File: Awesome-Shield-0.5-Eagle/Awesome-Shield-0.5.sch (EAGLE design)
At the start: 24 parts, among them J1 ARDUINO_R3_SHIELDUNO_R3_SHIEL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, SW1 SPST_TACT-EVQQ2

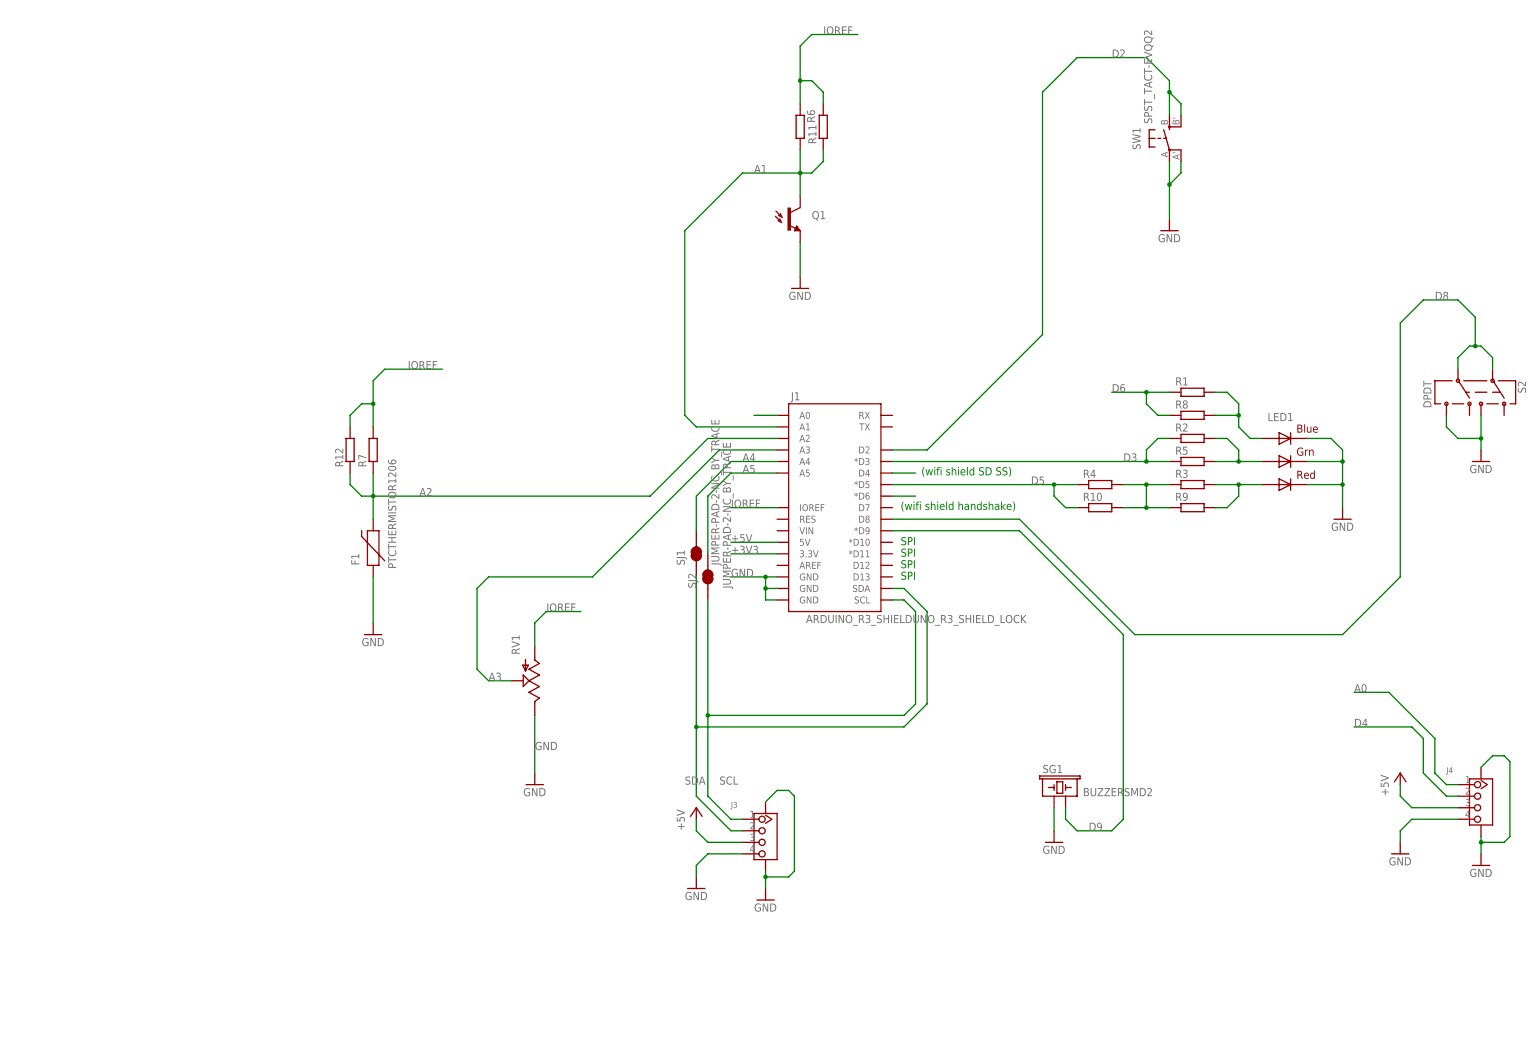
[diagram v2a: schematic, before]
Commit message: switched locking headers board for normal headers board
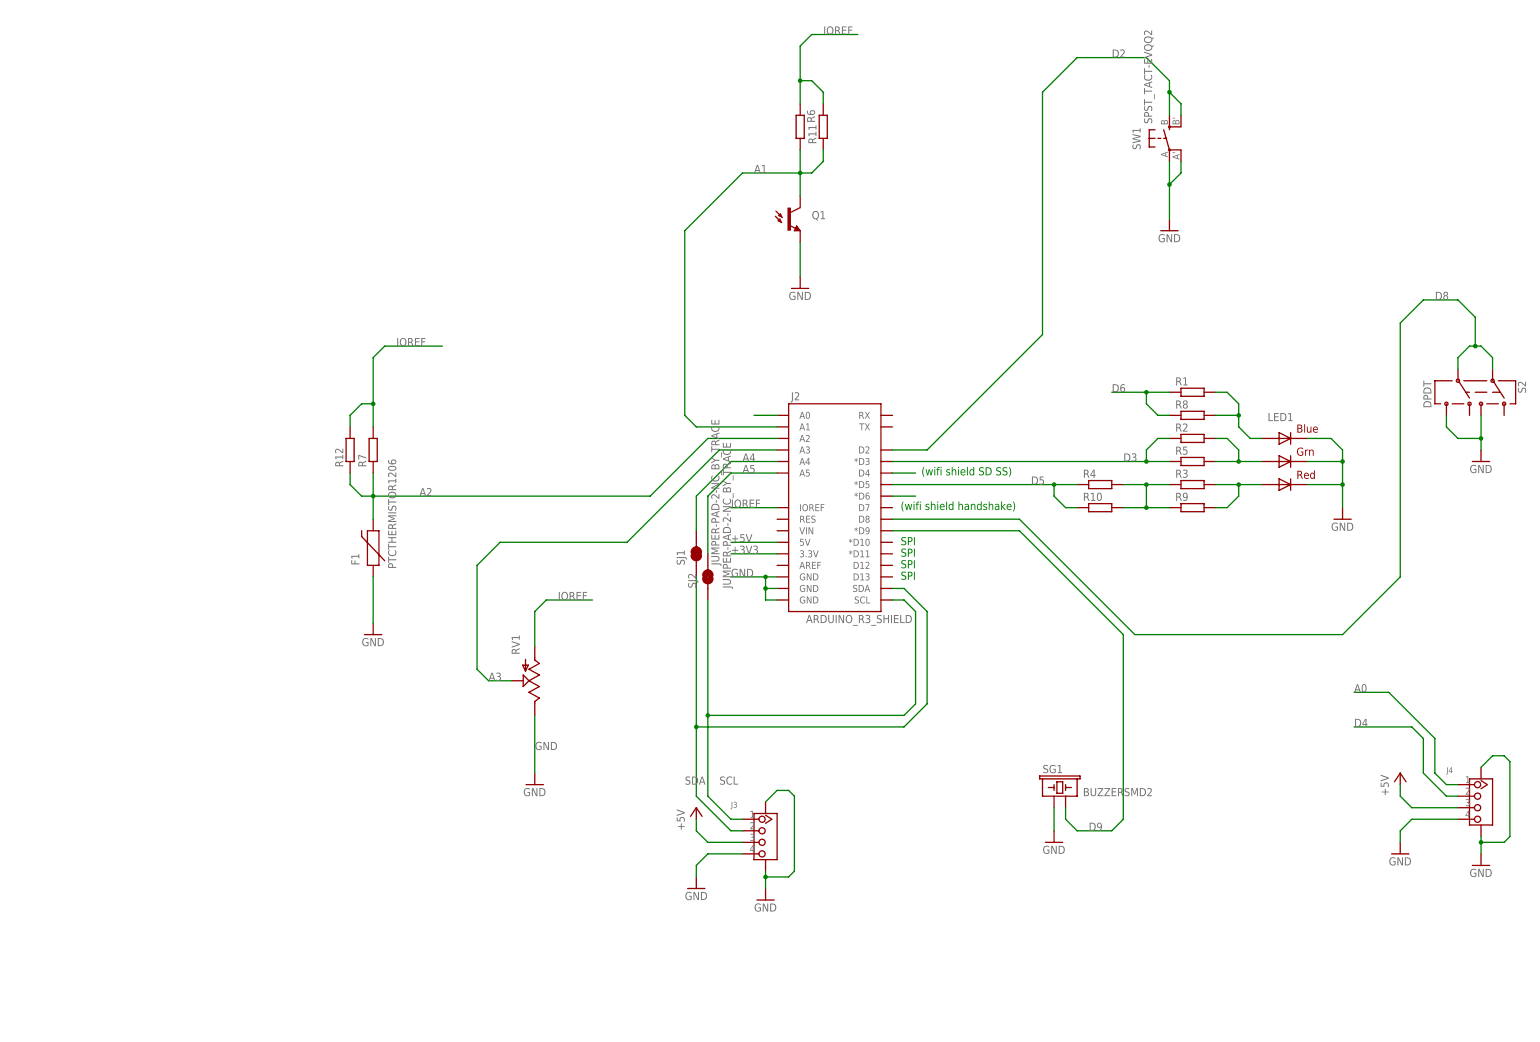
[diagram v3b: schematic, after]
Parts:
- removed J1: ARDUINO_R3_SHIELDUNO_R3_SHIELD_LOCK, SparkFun-Boards:ARDUINO_R3_SHIELDUNO_R3_SHIELD_LOCK
- added J2: ARDUINO_R3_SHIELD, SparkFun-Boards:ARDUINO_R3_SHIELD
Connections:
- net +3V3: now also J2.3.3V; no longer J1.3.3V
- net +5V: now also J2.5V; no longer J1.5V
- net A0: now also J2.A0; no longer J1.A0
- net A1: now also J2.A1; no longer J1.A1
- net A2: now also J2.A2; no longer J1.A2
- net A3: now also J2.A3; no longer J1.A3
- net A4: now also J2.A4; no longer J1.A4
- net A5: now also J2.A5; no longer J1.A5
- net D2: now also J2.D2; no longer J1.D2
- net D3: now also J2.*D3; no longer J1.*D3
- net D4: now also J2.D4; no longer J1.D4
- net D5: now also J2.*D5; no longer J1.*D5
- net D6: now also J2.*D6; no longer J1.*D6
- net D8: now also J2.D8; no longer J1.D8
- net D9: now also J2.*D9; no longer J1.*D9
- net GND: now also J2.GND@0, J2.GND@1, J2.GND@2; no longer J1.GND@0, J1.GND@1, J1.GND@2
- net IOREF: now also J2.IOREF; no longer J1.IOREF
- net SCL: now also J2.SCL; no longer J1.SCL
- net SDA: now also J2.SDA; no longer J1.SDA

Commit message: remove ground loops, move inputs to the left edge WIP
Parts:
- added FID1, FID2, FID3, FID4: FIDUCIAL1X2, SparkFun-Aesthetics:FIDUCIAL1X2
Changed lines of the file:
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@@
 <part name="J4" library="Seeed-OPL-Connector" deviceset="GROVE-CONNECTOR-SMD(4+2P-2.0)" device=""/>
 <part name="J2" library="SparkFun-Boards" deviceset="ARDUINO_R3_SHIELD" device=""/>
+<part name="FID1" library="SparkFun-Aesthetics" deviceset="FIDUCIAL" device="1X2"/>
+<part name="FID2" library="SparkFun-Aesthetics" deviceset="FIDUCIAL" device="1X2"/>
+<part name="FID3" library="SparkFun-Aesthetics" deviceset="FIDUCIAL" device="1X2"/>
+<part name="FID4" library="SparkFun-Aesthetics" deviceset="FIDUCIAL" device="1X2"/>
 </parts>
 <sheets>
@@
 <instance part="J4" gate="G$1" x="337.82" y="64.77"/>
 <instance part="J2" gate="G$1" x="195.58" y="132.08"/>
+<instance part="FID1" gate="G$1" x="294.64" y="30.48"/>
+<instance part="FID2" gate="G$1" x="299.72" y="30.48"/>
+<instance part="FID3" gate="G$1" x="304.8" y="30.48"/>
+<instance part="FID4" gate="G$1" x="309.88" y="30.48"/>
 </instances>
 <busses>

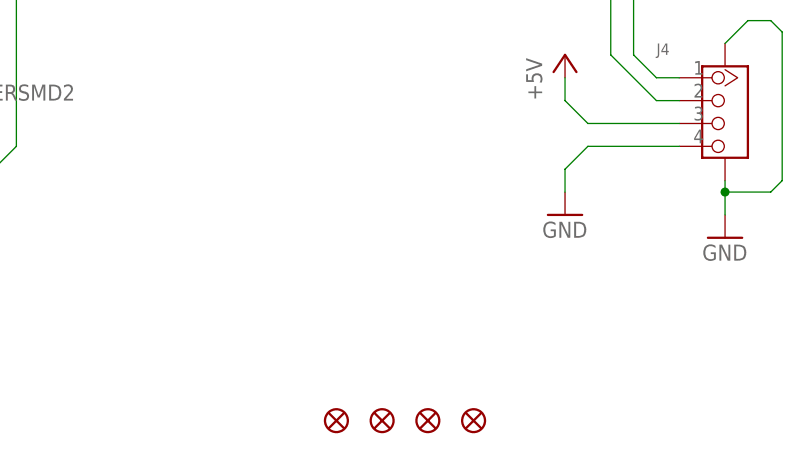
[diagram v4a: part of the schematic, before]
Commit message: change via sizes to .6mm, add micro fiducials
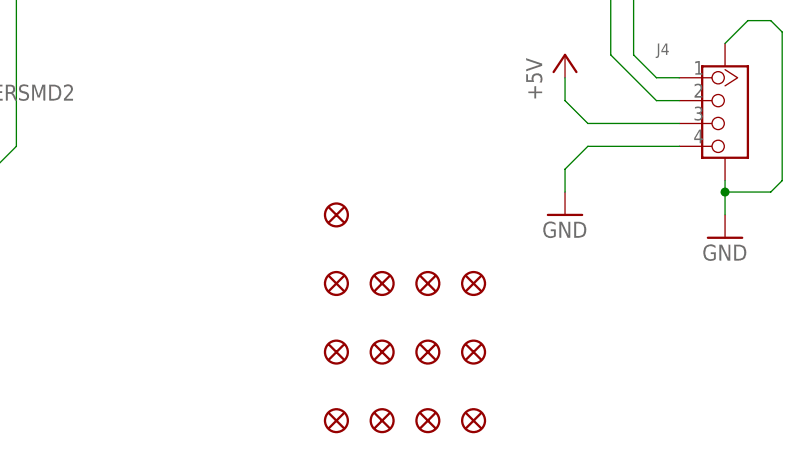
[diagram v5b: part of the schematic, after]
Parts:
- added FID10, FID11, FID12, FID13, FID5, FID6, FID7, FID8, FID9: FIDUCIALUFIDUCIAL, SparkFun-Aesthetics:FIDUCIALUFIDUCIAL
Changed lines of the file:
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@@
 <part name="FID3" library="SparkFun-Aesthetics" deviceset="FIDUCIAL" device="1X2"/>
 <part name="FID4" library="SparkFun-Aesthetics" deviceset="FIDUCIAL" device="1X2"/>
+<part name="FID5" library="SparkFun-Aesthetics" deviceset="FIDUCIAL" device="UFIDUCIAL"/>
+<part name="FID6" library="SparkFun-Aesthetics" deviceset="FIDUCIAL" device="UFIDUCIAL"/>
+<part name="FID7" library="SparkFun-Aesthetics" deviceset="FIDUCIAL" device="UFIDUCIAL"/>
+<part name="FID8" library="SparkFun-Aesthetics" deviceset="FIDUCIAL" device="UFIDUCIAL"/>
+<part name="FID9" library="SparkFun-Aesthetics" deviceset="FIDUCIAL" device="UFIDUCIAL"/>
+<part name="FID10" library="SparkFun-Aesthetics" deviceset="FIDUCIAL" device="UFIDUCIAL"/>
+<part name="FID11" library="SparkFun-Aesthetics" deviceset="FIDUCIAL" device="UFIDUCIAL"/>
+<part name="FID12" library="SparkFun-Aesthetics" deviceset="FIDUCIAL" device="UFIDUCIAL"/>
+<part name="FID13" library="SparkFun-Aesthetics" deviceset="FIDUCIAL" device="UFIDUCIAL"/>
 </parts>
 <sheets>
@@
 <instance part="FID3" gate="G$1" x="304.8" y="30.48"/>
 <instance part="FID4" gate="G$1" x="309.88" y="30.48"/>
+<instance part="FID5" gate="G$1" x="294.64" y="38.1"/>
+<instance part="FID6" gate="G$1" x="299.72" y="38.1"/>
+<instance part="FID7" gate="G$1" x="304.8" y="38.1"/>
+<instance part="FID8" gate="G$1" x="309.88" y="38.1"/>
+<instance part="FID9" gate="G$1" x="294.64" y="45.72"/>
+<instance part="FID10" gate="G$1" x="299.72" y="45.72"/>
+<instance part="FID11" gate="G$1" x="304.8" y="45.72"/>
+<instance part="FID12" gate="G$1" x="309.88" y="45.72"/>
+<instance part="FID13" gate="G$1" x="294.64" y="53.34"/>
 </instances>
 <busses>

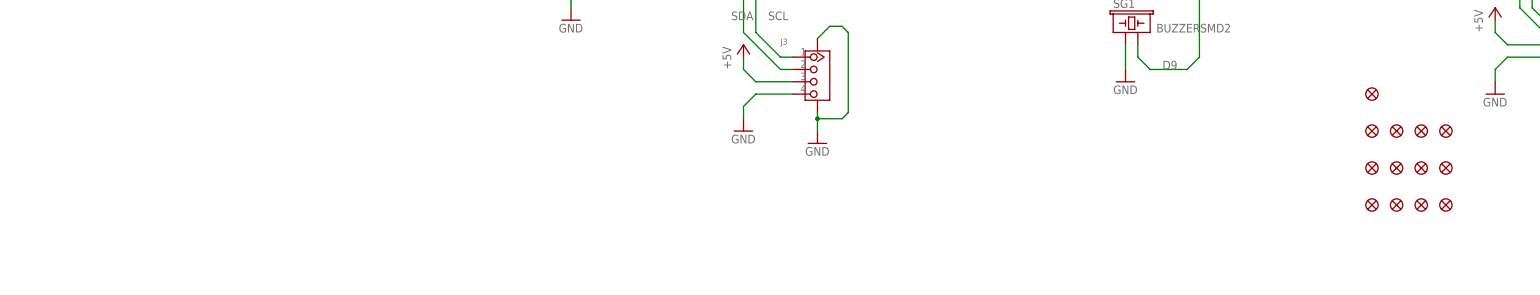
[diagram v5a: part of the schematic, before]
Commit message: adjusted fiducials as per issue 13
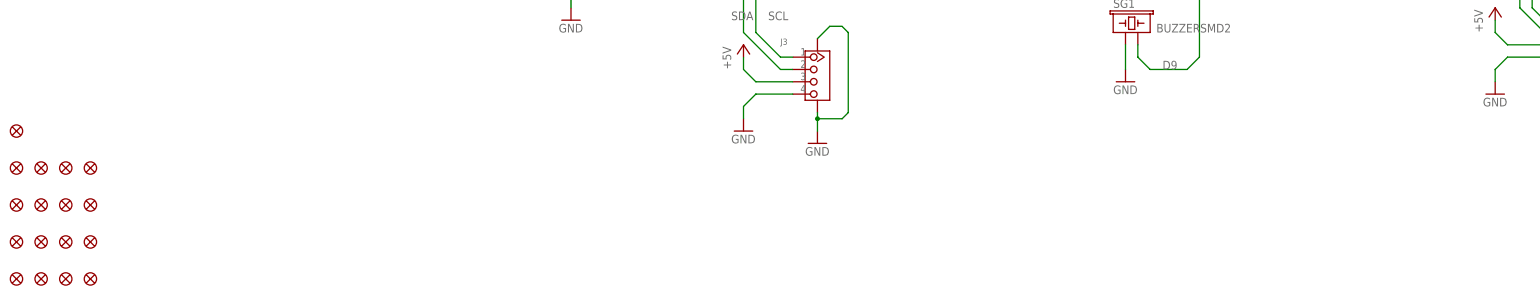
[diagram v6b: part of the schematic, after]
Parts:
- added FID15, FID16, FID17, FID18: FIDUCIALUFIDUCIAL, SparkFun-Aesthetics:FIDUCIALUFIDUCIAL
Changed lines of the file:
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@@
 <part name="FID12" library="SparkFun-Aesthetics" deviceset="FIDUCIAL" device="UFIDUCIAL"/>
 <part name="FID13" library="SparkFun-Aesthetics" deviceset="FIDUCIAL" device="UFIDUCIAL"/>
+<part name="FID15" library="SparkFun-Aesthetics" deviceset="FIDUCIAL" device="UFIDUCIAL"/>
+<part name="FID16" library="SparkFun-Aesthetics" deviceset="FIDUCIAL" device="UFIDUCIAL"/>
+<part name="FID17" library="SparkFun-Aesthetics" deviceset="FIDUCIAL" device="UFIDUCIAL"/>
+<part name="FID18" library="SparkFun-Aesthetics" deviceset="FIDUCIAL" device="UFIDUCIAL"/>
 </parts>
 <sheets>
@@
 <instance part="J4" gate="G$1" x="337.82" y="64.77"/>
 <instance part="J2" gate="G$1" x="195.58" y="132.08"/>
-<instance part="FID1" gate="G$1" x="294.64" y="30.48"/>
-<instance part="FID2" gate="G$1" x="299.72" y="30.48"/>
-<instance part="FID3" gate="G$1" x="304.8" y="30.48"/>
-<instance part="FID4" gate="G$1" x="309.88" y="30.48"/>
-<instance part="FID5" gate="G$1" x="294.64" y="38.1"/>
-<instance part="FID6" gate="G$1" x="299.72" y="38.1"/>
-<instance part="FID7" gate="G$1" x="304.8" y="38.1"/>
-<instance part="FID8" gate="G$1" x="309.88" y="38.1"/>
-<instance part="FID9" gate="G$1" x="294.64" y="45.72"/>
-<instance part="FID10" gate="G$1" x="299.72" y="45.72"/>
-<instance part="FID11" gate="G$1" x="304.8" y="45.72"/>
-<instance part="FID12" gate="G$1" x="309.88" y="45.72"/>
-<instance part="FID13" gate="G$1" x="294.64" y="53.34"/>
+<instance part="FID1" gate="G$1" x="15.24" y="15.24"/>
+<instance part="FID2" gate="G$1" x="20.32" y="15.24"/>
+<instance part="FID3" gate="G$1" x="25.4" y="15.24"/>
+<instance part="FID4" gate="G$1" x="30.48" y="15.24"/>
+<instance part="FID5" gate="G$1" x="15.24" y="22.86"/>
+<instance part="FID6" gate="G$1" x="20.32" y="22.86"/>
+<instance part="FID7" gate="G$1" x="25.4" y="22.86"/>
+<instance part="FID8" gate="G$1" x="30.48" y="22.86"/>
+<instance part="FID9" gate="G$1" x="15.24" y="30.48"/>
+<instance part="FID10" gate="G$1" x="20.32" y="30.48"/>
+<instance part="FID11" gate="G$1" x="25.4" y="30.48"/>
+<instance part="FID12" gate="G$1" x="30.48" y="30.48"/>
+<instance part="FID13" gate="G$1" x="15.24" y="38.1"/>
+<instance part="FID15" gate="G$1" x="25.4" y="38.1"/>
+<instance part="FID16" gate="G$1" x="30.48" y="38.1"/>
+<instance part="FID17" gate="G$1" x="15.24" y="45.72"/>
+<instance part="FID18" gate="G$1" x="20.32" y="38.1"/>
 </instances>
 <busses>

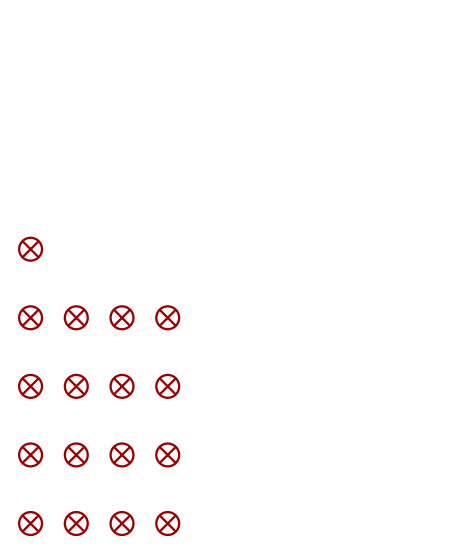
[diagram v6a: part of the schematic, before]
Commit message: fiducial placement now on a rectangular outline, silkscreen pulled away from the borders
don't forget to add the commit hash to the board on the backside.
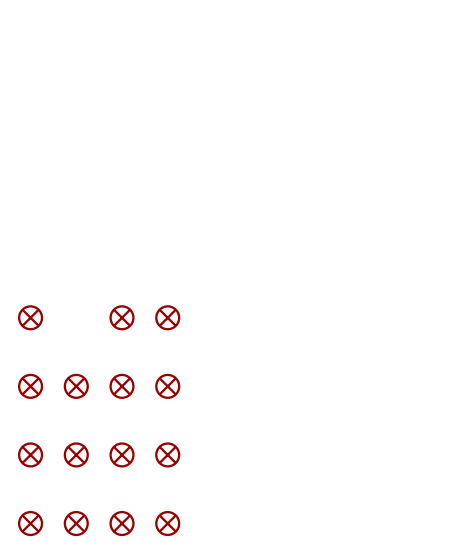
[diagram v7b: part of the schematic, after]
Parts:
- removed FID17, FID18: FIDUCIALUFIDUCIAL, SparkFun-Aesthetics:FIDUCIALUFIDUCIAL
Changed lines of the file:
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@@
 <part name="FID15" library="SparkFun-Aesthetics" deviceset="FIDUCIAL" device="UFIDUCIAL"/>
 <part name="FID16" library="SparkFun-Aesthetics" deviceset="FIDUCIAL" device="UFIDUCIAL"/>
-<part name="FID17" library="SparkFun-Aesthetics" deviceset="FIDUCIAL" device="UFIDUCIAL"/>
-<part name="FID18" library="SparkFun-Aesthetics" deviceset="FIDUCIAL" device="UFIDUCIAL"/>
 </parts>
 <sheets>
@@
 <instance part="FID15" gate="G$1" x="25.4" y="38.1"/>
 <instance part="FID16" gate="G$1" x="30.48" y="38.1"/>
-<instance part="FID17" gate="G$1" x="15.24" y="45.72"/>
-<instance part="FID18" gate="G$1" x="20.32" y="38.1"/>
 </instances>
 <busses>
